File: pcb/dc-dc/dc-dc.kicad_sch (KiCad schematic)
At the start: 21 parts, among them J1 sig_out, J2 sig_in, J3 Conn_01x02_Pin, J4 Conn_01x02_Pin, J5 Conn_01x02_Pin, J6 Conn_01x02_Pin, Q1 S8550, U1 TJA1051T-3, U2 LM2595S-3.3, U3 HX711

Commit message: update dc-dc
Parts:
- added C6: 330uF, symbol Device:C_Polarized
- added L1: 33uH, symbol Device:L
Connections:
- net GND: now also U2.3 (GND)
- no-connect marks 3 -> 4
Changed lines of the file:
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@@
+	)
+	(no_connect
+		(at 163.83 83.82)
 	)
 	(no_connect
@@
 	)
 	(symbol
+		(lib_id "Device:C_Polarized")
+		(at 148.59 85.09 0)
+		(unit 1)
+		(exclude_from_sim no)
+		(in_bom yes)
+		(on_board yes)
+		(dnp no)
+		(fields_autoplaced yes)
+		(property "Reference" "C6"
+			(at 152.4 82.9309 0)
+			(effects
+				(font
+					(size 1.27 1.27)
+				)
+				(justify left)
+			)
+		)
+		(property "Value" "330uF"
+			(at 152.4 85.4709 0)
+			(effects
+				(font
+					(size 1.27 1.27)
+				)
+				(justify left)
+			)
+		)
+		(property "Footprint" ""
+			(at 149.5552 88.9 0)
+			(effects
+				(font
+					(size 1.27 1.27)
+				)
+				(hide yes)
+			)
+		)
+		(property "Datasheet" "~"
+			(at 148.59 85.09 0)
+			(effects
+				(font
+					(size 1.27 1.27)
+				)
+				(hide yes)
+			)
+		)
+		(property "Description" "Polarized capacitor"
+			(at 148.59 85.09 0)
+			(effects
+				(font
+					(size 1.27 1.27)
+				)
+				(hide yes)
+			)
+		)
+		(pin "1"
+		)
+		(pin "2"
+		)
+		(instances
+			(project ""
+				(path "/59c3b22d-07f3-4a2c-af1b-a1c01316cf01"
+					(reference "C6")
+					(unit 1)
+				)
+			)
+		)
+	)
+	(symbol
 		(lib_id "Device:C")
 		(at 45.72 59.69 0)
@@
 	)
 	(symbol
+		(lib_id "Device:L")
+		(at 195.58 83.82 90)
+		(unit 1)
+		(exclude_from_sim no)
+		(in_bom yes)
+		(on_board yes)
+		(dnp no)
+		(fields_autoplaced yes)
+		(property "Reference" "L1"
+			(at 195.58 78.74 90)
+			(effects
+				(font
+					(size 1.27 1.27)
+				)
+			)
+		)
+		(property "Value" "33uH"
+			(at 195.58 81.28 90)
+			(effects
+				(font
+					(size 1.27 1.27)
+				)
+			)
+		)
+		(property "Footprint" ""
+			(at 195.58 83.82 0)
+			(effects
+				(font
+					(size 1.27 1.27)
+				)
+				(hide yes)
+			)
+		)
+		(property "Datasheet" "~"
+			(at 195.58 83.82 0)
+			(effects
+				(font
+					(size 1.27 1.27)
+				)
+				(hide yes)
+			)
+		)
+		(property "Description" "Inductor"
+			(at 195.58 83.82 0)
+			(effects
+				(font
+					(size 1.27 1.27)
+				)
+				(hide yes)
+			)
+		)
+		(pin "2"
+		)
+		(pin "1"
+		)
+		(instances
+			(project ""
+				(path "/59c3b22d-07f3-4a2c-af1b-a1c01316cf01"
+					(reference "L1")
+					(unit 1)
+				)
+			)
+		)
+	)
+	(symbol
 		(lib_id "power:GND")
 		(at 86.36 120.65 90)
@@
 					(unit 1)
 				)
+			)
+		)
+	)
+	(symbol
+		(lib_id "power:GND")
+		(at 176.53 88.9 0)
+		(unit 1)
+		(exclude_from_sim no)
+		(in_bom yes)
+		(on_board yes)
+		(dnp no)
+		(fields_autoplaced yes)
+		(property "Reference" "#PWR016"
+			(at 176.53 95.25 0)
+			(effects
+				(font
+					(size 1.27 1.27)
+				)
+				(hide yes)
+			)
+		)
+		(property "Value" "GND"
+			(at 176.53 93.98 0)
+			(effects
+				(font
+					(size 1.27 1.27)
+				)
+			)
+		)
+		(property "Footprint" ""
+			(at 176.53 88.9 0)
+			(effects
+				(font
+					(size 1.27 1.27)
+				)
+				(hide yes)
+			)
+		)
+		(property "Datasheet" ""
+			(at 176.53 88.9 0)
+			(effects
+				(font
+					(size 1.27 1.27)
+				)
+				(hide yes)
+			)
+		)
+		(property "Description" "Power symbol creates a global label with name \"GND\" , ground"
+			(at 176.53 88.9 0)
+			(effects
+				(font
+					(size 1.27 1.27)
+				)
+				(hide yes)
+			)
+		)
+		(pin "1"
+		)
+		(instances
+			(project ""
+				(path "/59c3b22d-07f3-4a2c-af1b-a1c01316cf01"
+					(reference "#PWR016")
+					(unit 1)
+				)

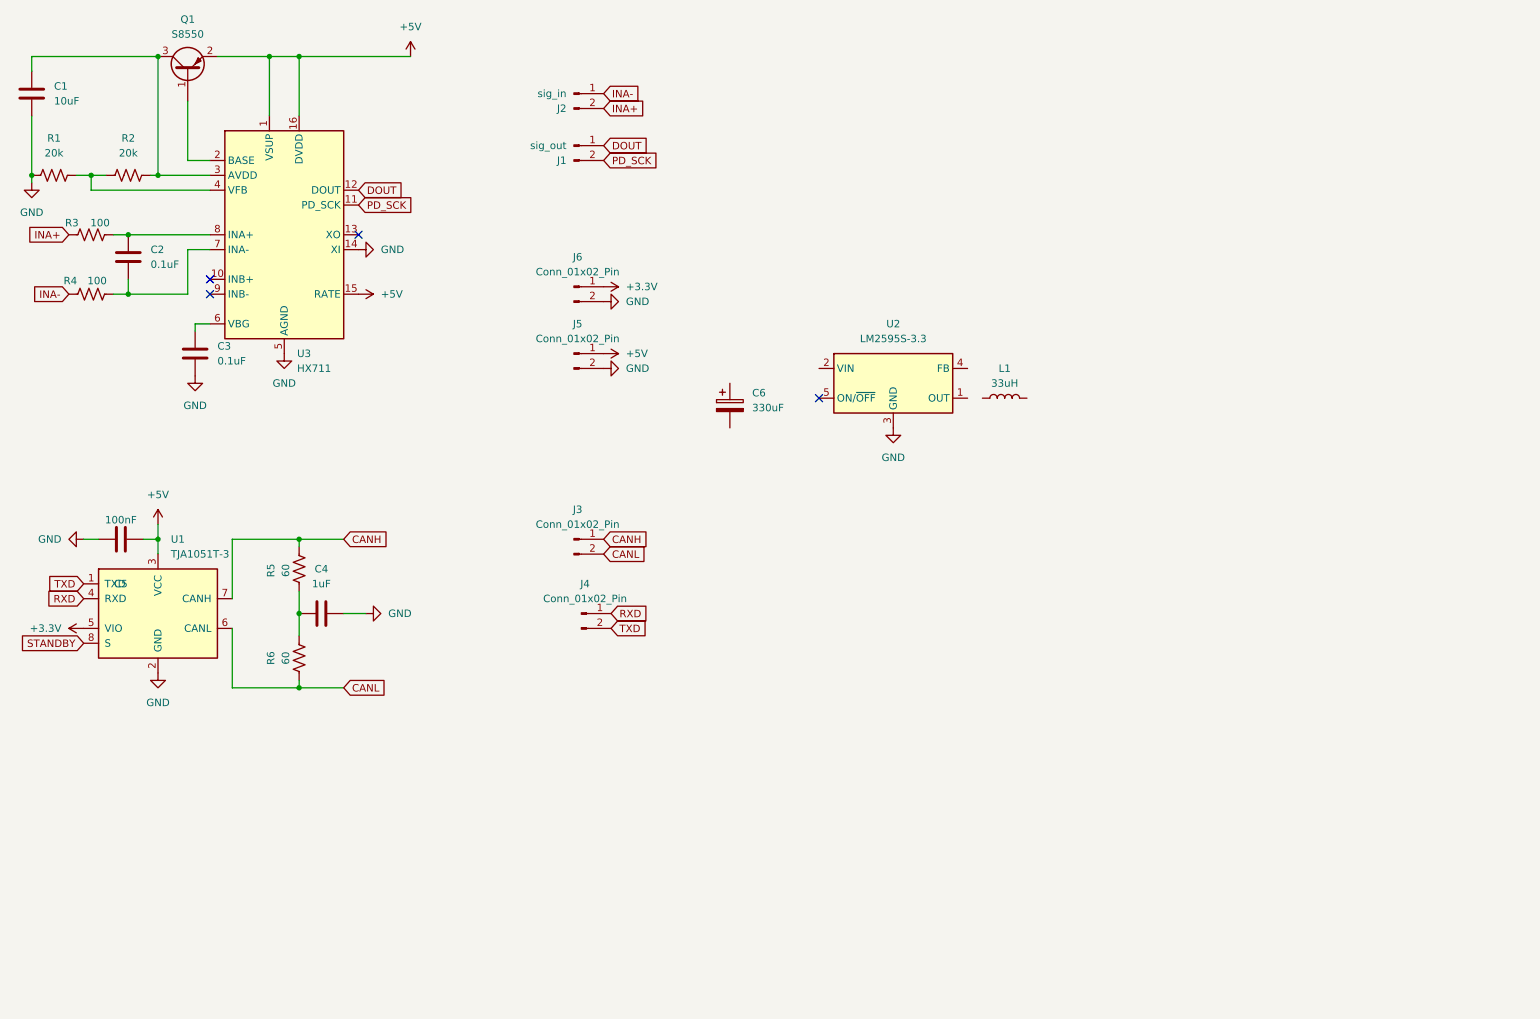
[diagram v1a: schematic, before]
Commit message: update dc-dc
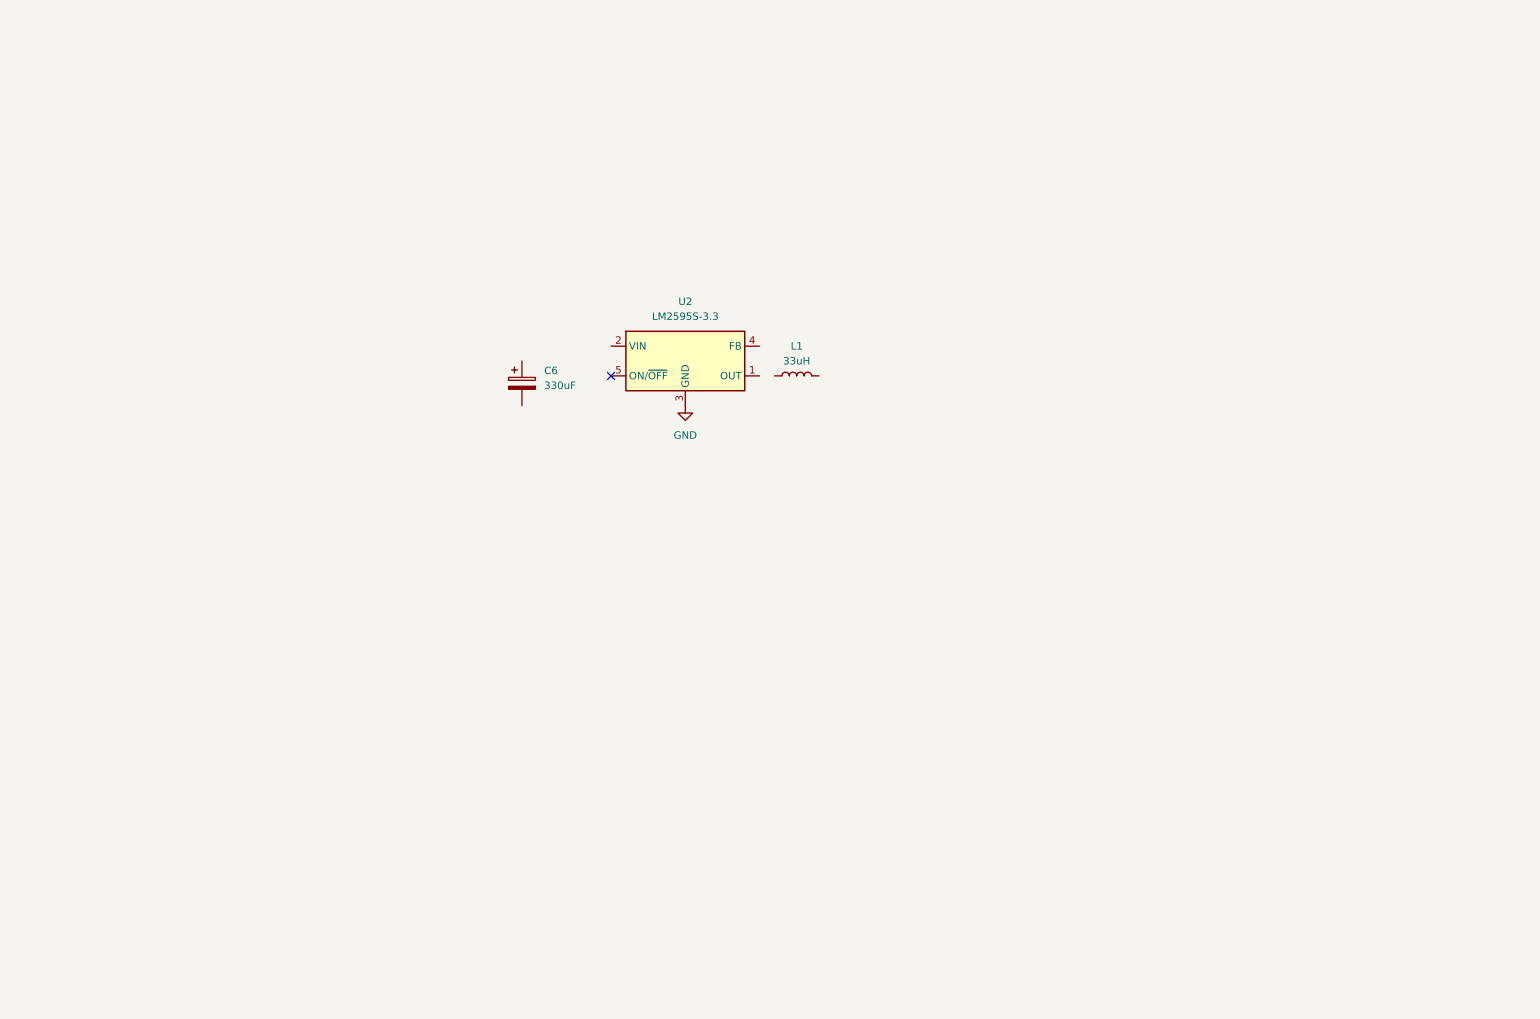
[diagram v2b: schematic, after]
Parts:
- removed C1: 10uF, symbol Device:C
- removed C2, C3: 0.1uF, symbol Device:C
- removed C4: 1uF, symbol Device:C
- removed C5: 100nF, symbol Device:C
- removed J1: sig_out, symbol Connector:Conn_01x02_Pin
- removed J2: sig_in, symbol Connector:Conn_01x02_Pin
- removed J3, J4, J5, J6: Conn_01x02_Pin, symbol Connector:Conn_01x02_Pin
- removed Q1: S8550, Package_TO_SOT_SMD:SOT-23, symbol Transistor_BJT:SS8550
- removed R1, R2: 20k, symbol Device:R_US
- removed R3, R4: 100, symbol Device:R_US
- removed R5, R6: 60, symbol Device:R_US
- removed U1: TJA1051T-3, Package_SO:SOIC-8_3.9x4.9mm_P1.27mm, symbol Interface_CAN_LIN:TJA1051T-3
- removed U3: HX711, Package_SO:SOP-16_3.9x9.9mm_P1.27mm, symbol Analog_ADC:HX711
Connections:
- no-connect marks 4 -> 1
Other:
- moved on the sheet: C6, L1, U2

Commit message: update
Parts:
- added C1: 220uF, symbol Device:C_Polarized
- added C2, C4: 2.2uF, symbol Device:C
- added C3: 100nF, symbol Device:C
- added D1, D2: ss53c, symbol Device:D_Schottky
- added L2: 33uH, symbol Device:L
- added U1: LM2595S-5, Package_TO_SOT_SMD:TO-263-5_TabPin3, symbol Regulator_Switching:LM2595S-5
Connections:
- net GND: now also C6.2, C1.2, C2.1, C3.1, C4.1, D1.2 (A), D2.2 (A), U1.3 (GND)
- net at C6.1: now also L1.2, U2.4 (FB)
- net at L1.1: now also U2.1 (OUT), D1.1 (K)
- net VIN_MAX40V: now reaches U2.2 (VIN)
- net VIN_MAX40V: now also C2.2, C3.2, C4.2, U1.2 (VIN)
- new net: D2.1 (K), L2.1, U1.1 (OUT)
- new net: C1.1, L2.2, U1.4 (FB)
- no-connect marks 1 -> 2
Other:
- moved on the sheet: C6, L1

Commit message: feat: update
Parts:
- removed C1: 220uF, symbol Device:C_Polarized
- removed C2, C4: 2.2uF, symbol Device:C
- removed C3: 100nF, symbol Device:C
- removed C6: 330uF, symbol Device:C_Polarized
- removed D1, D2: ss53c, symbol Device:D_Schottky
- removed L1, L2: 33uH, symbol Device:L
- removed U1: LM2595S-5, Package_TO_SOT_SMD:TO-263-5_TabPin3, symbol Regulator_Switching:LM2595S-5
- removed U2: LM2595S-3.3, Package_TO_SOT_SMD:TO-263-5_TabPin3, symbol Regulator_Switching:LM2595S-3.3
- added C54, C55, C56: 4.7uf/50v, Capacitor_SMD:C_1206_3216Metric, symbol Device:C
- added C57, C59: 100nf/50v, Capacitor_SMD:C_0603_1608Metric, symbol Device:C
- added C58, C60: 10uf/50v, Capacitor_SMD:C_1210_3225Metric, symbol Device:C
- added C61: 68nF, Capacitor_SMD:C_0603_1608Metric, symbol Device:C
- added C62, C63: 47nF, Capacitor_SMD:C_0603_1608Metric, symbol Device:C
- added C64, C65, C66: 100nF/16v, Capacitor_SMD:C_0603_1608Metric, symbol Device:C
- added C67, C68: 10uF/35v, Capacitor_SMD:C_1210_3225Metric, symbol Device:C
- added C69, C70: 10uF/16v, Capacitor_SMD:C_1210_3225Metric, symbol Device:C
- added C71, C72: 10uF/10v, Capacitor_SMD:C_0603_1608Metric, symbol Device:C
- added D28, D29, D30: B560C, Diode_SMD:D_SMC, symbol Device:D_Schottky
- added L5, L7: 22uH, Inductor_SMD:L_TDK_SLF12565, symbol Device:L
- added L6: 47uH, Inductor_SMD:L_TDK_SLF12565, symbol Device:L
- added R103, R104: 1.3k, Resistor_SMD:R_0603_1608Metric, symbol Device:R_US
- added R105: 100k, Resistor_SMD:R_0603_1608Metric, symbol Device:R_US
- added R106, R107: 62k, Resistor_SMD:R_0603_1608Metric, symbol Device:R_US
- added R108: 300k, Resistor_SMD:R_0603_1608Metric, symbol Device:R_US
- added R109, R110, R113, R116: 10k, Resistor_SMD:R_0603_1608Metric, symbol Device:R_US
- added R111: 56k, Resistor_SMD:R_0603_1608Metric, symbol Device:R_US
- added R112: 680, Resistor_SMD:R_0603_1608Metric, symbol Device:R_US
- added R114: 33k, Resistor_SMD:R_0603_1608Metric, symbol Device:R_US
- added R115: 1k, Resistor_SMD:R_0603_1608Metric, symbol Device:R_US
- added U14, U15, U16: LMR16030SDDAR, Package_SO:TI_SO-PowerPAD-8_ThermalVias, symbol 2025-01-08_11-11-09:LMR16030SDDAR
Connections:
- net GND: now also C54.2, C55.1, C56.1, C57.2, C58.2, C59.2, C60.1, C61.2, C62.2, C63.2, C67.2, C68.1, C69.2, C70.1, C71.2, C72.1, D28.2 (A), D29.2 (A), D30.2 (A), R103.2, R104.2, R105.2, R110.2, R113.2, R116.2, U14.7 (GND), U14.9 (EP), U15.7 (GND), U15.9 (EP), U16.7 (GND), U16.9 (EP)
- new net: C62.1, U15.6 (SS/PGOOD)
- new net: D28.1 (K), L5.1, U14.8 (SW)
- new net: C66.2, U16.1 (BOOT)
- new net: R107.1, U16.4 (RT/YNC)
- new net: R115.2, R116.1, U16.5 (FB)
- new net: C63.1, U16.6 (SS/PGOOD)
- new net: D30.1 (K), L7.1, U16.8 (SW)
- new net: R108.2, R109.1
- new net: C64.2, U14.1 (BOOT)
- new net: R105.1, U14.4 (RT/YNC)
- new net: R109.2, R110.1, U14.5 (FB)
- new net: C61.1, U14.6 (SS/PGOOD)
- new net: C65.2, U15.1 (BOOT)
- new net: R103.1, R106.2
- new net: R112.2, R113.1, U15.5 (FB)
- new net: D29.1 (K), L6.1, U15.8 (SW)
- new net: R106.1, U15.4 (RT/YNC)
- new net: R104.1, R107.2
- new net: R114.2, R115.1
- new net: R111.2, R112.1
- new net 24V/3A: C54.1, C55.2, C56.2, C57.1, C64.1, C67.1, C68.2, L5.2, R108.1, U15.2 (VIN), U16.2 (VIN)
- new net 3.3V/3A: C66.1, C71.1, C72.2, L7.2, R114.1
- new net 5V/3A: C65.1, C69.1, C70.2, L6.2, R111.1
- new net VIN_MAX60V: C58.1, C59.1, C60.2, U14.2 (VIN)
- no-connect marks 2 -> 3

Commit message: feat: update
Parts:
- added D13, D14, D17: LED, LED_SMD:LED_0603_1608Metric, symbol Device:LED
- added J8: power, Connector_AMASS:AMASS_XT60PW-M_1x02_P7.20mm_Horizontal, symbol Connector:Conn_01x02_Pin
- added R19, R20, R23: 10k, Resistor_SMD:R_0603_1608Metric, symbol Device:R_US
- renumbered C60 to C10, C61 to C11, C65 to C12, C64 to C13, C69 to C14, C70 to C15, C67 to C16, C68 to C17, C63 to C18, C66 to C19, C54 to C20, C55 to C21, C71 to C22, C72 to C23, C56 to C24, C57 to C25, C58 to C7, C59 to C8, C62 to C9, D29 to D11, D28 to D12, D30 to D16, L6 to L1, L5 to L2, L7 to L3, R103 to R10, R106 to R11, R105 to R12, R111 to R13, R112 to R14, R113 to R15, R108 to R16, R109 to R17, R110 to R18, R104 to R21, R107 to R22, R114 to R24, R115 to R25, R116 to R26, U15 to U4, U14 to U5, U16 to U6
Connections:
- net 24V/3A: no longer U6.2 (VIN)
- net GND: now also J8.2 (Pin_2), R19.2, R20.2, R23.2
- net VIN_MAX60V renamed VCC
- net VCC: now also J8.1 (Pin_1)
- new net: D14.1 (K), R20.1
- new net: D13.1 (K), R19.1
- new net: D17.1 (K), R23.1
- new net +24V: D13.2 (A)
- new net +3.3V: D17.2 (A)
- new net +5V: D14.2 (A), U6.2 (VIN)
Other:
- note added: "LMR16030SDDAR max input 60V but BTN8982TA max input 45V so final max VCC input is 45V"
- moved on the sheet: C20, C21, C24, C25

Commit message: feat: update
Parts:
- removed C21, C24: 4.7uf/50v, Capacitor_SMD:C_1206_3216Metric, symbol Device:C
- added 3.3V4: LED, LED_SMD:LED_0603_1608Metric, symbol Device:LED
- added C47, C48: 220uf, Capacitor_SMD:CP_Elec_10x10.5, symbol Device:C_Polarized
- added R56: 10k, Resistor_SMD:R_0603_1608Metric, symbol Device:R_US
- renumbered L3 to L2, L2 to L3, U6 to U5, U5 to U6
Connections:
- net 24V/3A: now also C20.2; no longer C20.1
- net GND: now also C20.1, 3.3V4.1 (K), C47.2, C48.2; no longer C20.2
- net VCC: now also C47.1, C48.1, R56.1
- new net: 3.3V4.2 (A), R56.2
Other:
- moved on the sheet: C20, C25, D13, D14, D17, R19, R20, R23

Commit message: feat: update
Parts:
- removed C47: 220uf, Capacitor_SMD:CP_Elec_10x10.5, symbol Device:C_Polarized
- 3.3V4: value LED -> VCC
- D13: value LED -> +24V
- D14: value LED -> +5V
- D17: value LED -> +3.3V
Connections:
- net +24V is gone; now on net 24V/3A: D13.2 (A)
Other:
- moved on the sheet: C12, C14, C15, C20, C25, C48, C9, D11, D13, D14, D17, L1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
